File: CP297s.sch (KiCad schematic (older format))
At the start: 125 parts, among them J1 Conn_01x05_Male, J2 Conn_01x04_Female, J3 pin header 01x15 2.54mm, J4 Conn_01x06_Female, J5 PG203J, J6 PG203J, J7 PG203J, K1 CONN_3, K2 CONN_3, K3 TK85_BUS, P2 CONN_2, P6 CONN_2, SW1 SW_SPDT, U1 Z80, U10 74LS125, U11 74LS393, U12 74LS574, U13 74LS08, U14 74LS251, U15 74HC86, U16 74LS245, U17 74LS32, U18 74HCT00, U19 74LS138, U2 62256, U20 74HC74, U21 74HC74, U22 74LS165, U23 74LS32, U24 AY-3-8910, U25 74LS08, U26 74LS138, U3 27256, U4 74HC04, U5 74HC74, U6 74LS393, U7 74LS11, U8 74LS32, U9 74LS245, X1 6.5MHz

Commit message: Added header for Tek V2
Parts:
- added J8: Conn_01x03_Female, Connector_PinHeader_2.54mm:PinHeader_1x03_P2.54mm_Vertical, symbol Connector_Generic:Conn_01x03_Female
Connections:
- net +5V: now also J8.1 (Pin_1)
- net ~KBD: now also J8.3 (Pin_3)
- net ~WAIT: now also J8.2 (Pin_2)
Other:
- note added: "50/60HZ\nJUMPER"
- note added: "Tek V2"
- note removed: "50HZ\nJUMPER"
- moved on the sheet: C4, P6, R32
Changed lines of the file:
@@
 	1    0    0    -1
 $EndComp
-Text Label 7700 8650 0    50   ~ 0
-INVERT
 Text GLabel 1000 10100 0    50   Output ~ 0
 NOP
@@
 L CP297s:GND-CP297s #PWR032
 U 1 1 51BD612C
-P 13750 18600
-F 0 "#PWR032" H 13750 18600 30  0001 C CNN
-F 1 "GND" H 13750 18530 30  0001 C CNN
-F 2 "" H 13750 18600 60  0000 C CNN
-F 3 "" H 13750 18600 60  0000 C CNN
-	1    13750 18600
+P 13750 18650
+F 0 "#PWR032" H 13750 18650 30  0001 C CNN
+F 1 "GND" H 13750 18580 30  0001 C CNN
+F 2 "" H 13750 18650 60  0000 C CNN
+F 3 "" H 13750 18650 60  0000 C CNN
+	1    13750 18650
 	1    0    0    -1
 $EndComp
@@
 L CP297s:CONN_2-CP297s P6
 U 1 1 51BD634C
-P 14100 19200
-F 0 "P6" V 14050 19200 40  0000 C CNN
-F 1 "CONN_2" V 14150 19200 40  0000 C CNN
-F 2 "Connector_PinHeader_2.54mm:PinHeader_1x02_P2.54mm_Vertical" H 14100 19200 60  0001 C CNN
-F 3 "" H 14100 19200 60  0000 C CNN
-	1    14100 19200
+P 13750 18950
+F 0 "P6" V 13700 18950 40  0000 C CNN
+F 1 "CONN_2" V 13800 18950 40  0000 C CNN
+F 2 "Connector_PinHeader_2.54mm:PinHeader_1x02_P2.54mm_Vertical" H 13750 18950 60  0001 C CNN
+F 3 "" H 13750 18950 60  0000 C CNN
+	1    13750 18950
 	1    0    0    -1
 $EndComp
@@
 L CP297s:GND-CP297s #PWR033
 U 1 1 51BD6358
-P 13750 19350
-F 0 "#PWR033" H 13750 19350 30  0001 C CNN
-F 1 "GND" H 13750 19280 30  0001 C CNN
-F 2 "" H 13750 19350 60  0000 C CNN
-F 3 "" H 13750 19350 60  0000 C CNN
-	1    13750 19350
+P 13400 19200
+F 0 "#PWR033" H 13400 19200 30  0001 C CNN
+F 1 "GND" H 13400 19130 30  0001 C CNN
+F 2 "" H 13400 19200 60  0000 C CNN
+F 3 "" H 13400 19200 60  0000 C CNN
+	1    13400 19200
 	-1   0    0    -1
 $EndComp
-Text Notes 14250 19150 0    50   ~ 0
-50HZ\nJUMPER
+Text Notes 13900 19050 0    50   ~ 0
+50{slash}60HZ\nJUMPER
 $Comp
 L CP297s:GND-CP297s #PWR036
@@
 L CP297s:R-CP297s R32
 U 1 1 51BD6B09
-P 13250 19200
-F 0 "R32" V 13330 19200 40  0000 C CNN
-F 1 "180" V 13257 19201 40  0000 C CNN
-F 2 "Resistor_THT:R_Axial_DIN0207_L6.3mm_D2.5mm_P7.62mm_Horizontal" V 13180 19200 30  0001 C CNN
-F 3 "~" H 13250 19200 30  0001 C CNN
-	1    13250 19200
+P 13150 19200
+F 0 "R32" V 13230 19200 40  0000 C CNN
+F 1 "180" V 13157 19201 40  0000 C CNN
+F 2 "Resistor_THT:R_Axial_DIN0207_L6.3mm_D2.5mm_P7.62mm_Horizontal" V 13080 19200 30  0001 C CNN
+F 3 "~" H 13150 19200 30  0001 C CNN
+	1    13150 19200
 	1    0    0    -1
 $EndComp
@@
 L CP297s:C-CP297s C4
 U 1 1 51BD6B0F
-P 13250 19750
-F 0 "C4" H 13250 19850 40  0000 L CNN
-F 1 "47n" H 13256 19665 40  0000 L CNN
-F 2 "Capacitor_THT:C_Disc_D7.0mm_W2.5mm_P5.00mm" H 13288 19600 30  0001 C CNN
-F 3 "~" H 13250 19750 60  0001 C CNN
-	1    13250 19750
+P 13150 19750
+F 0 "C4" H 13150 19850 40  0000 L CNN
+F 1 "47n" H 13156 19665 40  0000 L CNN
+F 2 "Capacitor_THT:C_Disc_D7.0mm_W2.5mm_P5.00mm" H 13188 19600 30  0001 C CNN
+F 3 "~" H 13150 19750 60  0001 C CNN
+	1    13150 19750
 	1    0    0    -1
 $EndComp
@@
 	12700 18550 13750 18550
 Wire Wire Line
-	13750 18550 13750 18600
-Wire Wire Line
-	13750 19300 13750 19350
+	13750 18550 13750 18650
 Wire Wire Line
-	13650 19100 13750 19100
+	13400 19050 13400 19200
 Wire Wire Line
 	12700 18650 13400 18650
@@
 	12800 19450 12800 19550
 Wire Wire Line
-	13250 18750 13250 18950
+	13150 18750 13150 18950
 Connection ~ 12800 18750
 Wire Wire Line
-	13250 19550 13250 19450
+	13150 19550 13150 19450
 Wire Wire Line
 	12450 20500 12450 20400
@@
 	12050 6450 11550 6450
 Wire Wire Line
-	12800 18750 13250 18750
+	12800 18750 13150 18750
 Wire Wire Line
 	12450 20400 12750 20400
@@
 Wire Wire Line
 	6900 18100 7000 18100
-Text Label 1100 19550 0    50   ~ 0
-~IOWR
 Wire Wire Line
 	4300 5050 4450 5050
@@
 AUDIO-MONO
 Wire Wire Line
-	13900 20500 13250 20500
+	13900 20500 13150 20500
 Wire Wire Line
-	13250 19950 13250 20500
+	13150 19950 13150 20500
 Wire Wire Line
 	14300 20700 14300 20900
@@
 	13400 17950 13400 18650
 Connection ~ 13400 18650
-Wire Wire Line
-	13400 18650 13650 18650
-Wire Wire Line
-	13650 18650 13650 19100
 $Comp
 L CP297s:DIODE-CP297s D12
@@
 	14900 1600 15100 1600
 Connection ~ 14900 1600
+Wire Wire Line
+	13400 18650 13400 18850
+Text Notes 15100 19000 0    50   ~ 0
+Tek V2
+$Comp
+L Connector_Generic:Conn_01x03_Female J8
+U 1 1 5D57DF26
+P 14950 18950
+F 0 "J8" H 14978 18976 50  0000 L CNN
+F 1 "Conn_01x03_Female" H 14978 18885 50  0000 L CNN
+F 2 "Connector_PinHeader_2.54mm:PinHeader_1x03_P2.54mm_Vertical" H 14950 18950 50  0001 C CNN
+F 3 "~" H 14950 18950 50  0001 C CNN
+	1    14950 18950
+	1    0    0    -1
+$EndComp
+Wire Wire Line
+	14750 19050 14650 19050
+Wire Wire Line
+	14750 18950 14550 18950
+Wire Wire Line
+	14750 18850 14650 18850
+Wire Wire Line
+	14650 18850 14650 18800
+$Comp
+L CP297s:+5V-CP297s #PWR0112
+U 1 1 5D5A98AB
+P 14650 18800
+F 0 "#PWR0112" H 14650 18890 20  0001 C CNN
+F 1 "+5V" H 14650 18890 30  0000 C CNN
+F 2 "" H 14650 18800 60  0001 C CNN
+F 3 "" H 14650 18800 60  0001 C CNN
+	1    14650 18800
+	1    0    0    -1
+$EndComp
+Text GLabel 14550 18950 0    50   Input ~ 0
+~WAIT
+Wire Wire Line
+	14650 19050 14650 19150
+Wire Wire Line
+	14650 19150 14550 19150
+Text GLabel 14550 19150 0    50   Input ~ 0
+~KBD
+Text GLabel 7950 8650 2    50   Input ~ 0
+INVERT
+Wire Wire Line
+	7950 8650 7800 8650
+Connection ~ 7800 8650
+Text GLabel 1100 19550 0    50   Input ~ 0
+~IOWR
 $EndSCHEMATC

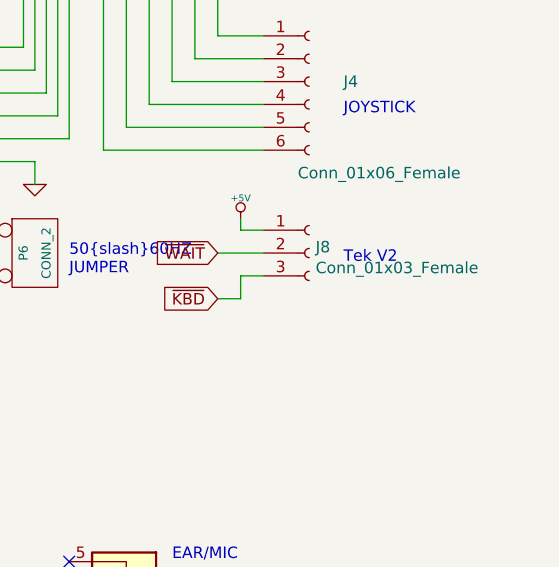
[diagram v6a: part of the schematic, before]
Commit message: Aesthetic improvement, gerbers added
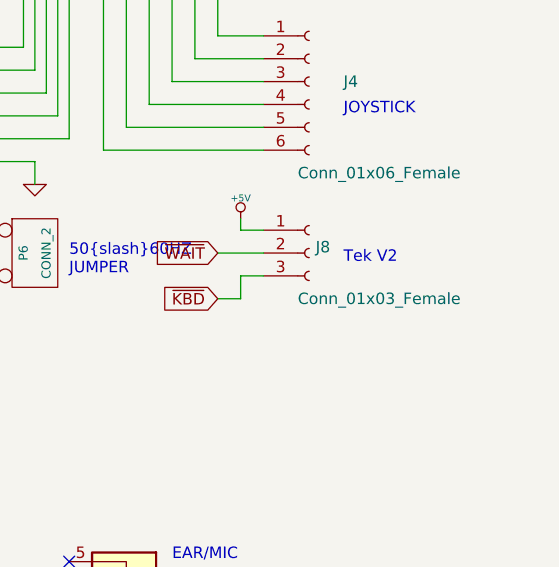
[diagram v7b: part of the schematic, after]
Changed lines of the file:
@@
 P 14950 18950
 F 0 "J8" H 14978 18976 50  0000 L CNN
-F 1 "Conn_01x03_Female" H 14978 18885 50  0000 L CNN
+F 1 "Conn_01x03_Female" H 14900 18750 50  0000 L CNN
 F 2 "Connector_PinHeader_2.54mm:PinHeader_1x03_P2.54mm_Vertical" H 14950 18950 50  0001 C CNN
 F 3 "~" H 14950 18950 50  0001 C CNN
